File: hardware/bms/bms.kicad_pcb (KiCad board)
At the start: 4 copper layers, 120 x 45 mm, 287 parts, among them J1 Screw_Terminal_01x01, J10 Conn_01x10, J11 USB_C_Receptacle_USB2.0, J12 Conn_01x03, J13 Conn_01x07, J2 Screw_Terminal_01x01, J3 Screw_Terminal_01x01, J4 Screw_Terminal_01x01, J5 Screw_Terminal_01x01, J6 Conn_01x02, J7 Conn_01x10, J8 Conn_01x02, J9 Micro_SD_Card_Det2, Q1 MMBT3904, Q2 Q_PMOS_GSD, Q3 Q_PMOS_GSD, Q4 BSZ018N04LS6ATMA1, Q5 IAUC120N04S6N006ATMA1, Q6 IAUC120N04S6N006ATMA1, Q7 BSZ018N04LS6ATMA1, Q8 BSZ018N04LS6ATMA1, Q9 BSZ018N04LS6ATMA1, SW1 SW_SPST, SW2 SW_Push, SW3 SW_Push, U1 BQ76952, U2 LM74700, U3 BQ24610, U4 LM5166X, U5 TPS62172DSG, U6 ESP32-C3-MINI-1-N4, U8 USBLC6-2SC6, U9 TXU0101DCKR

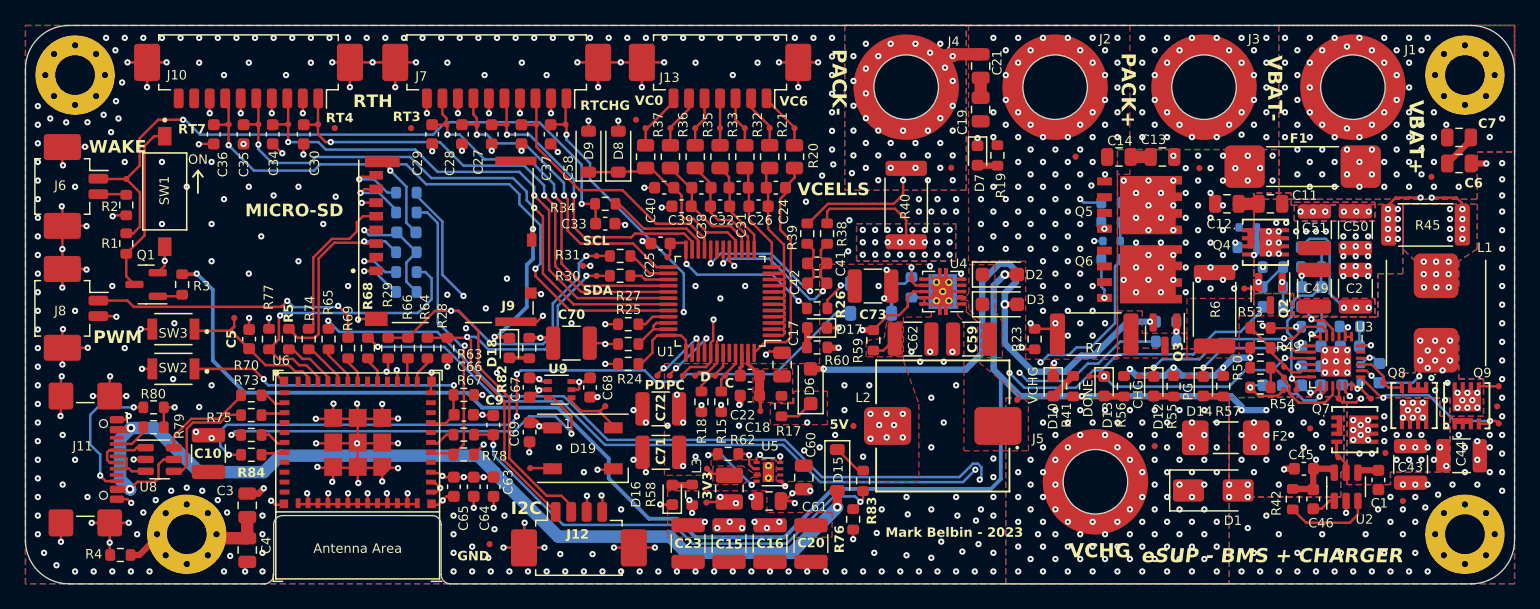
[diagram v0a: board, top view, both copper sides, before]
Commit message: Added keystone clip test points for ground, should be nice
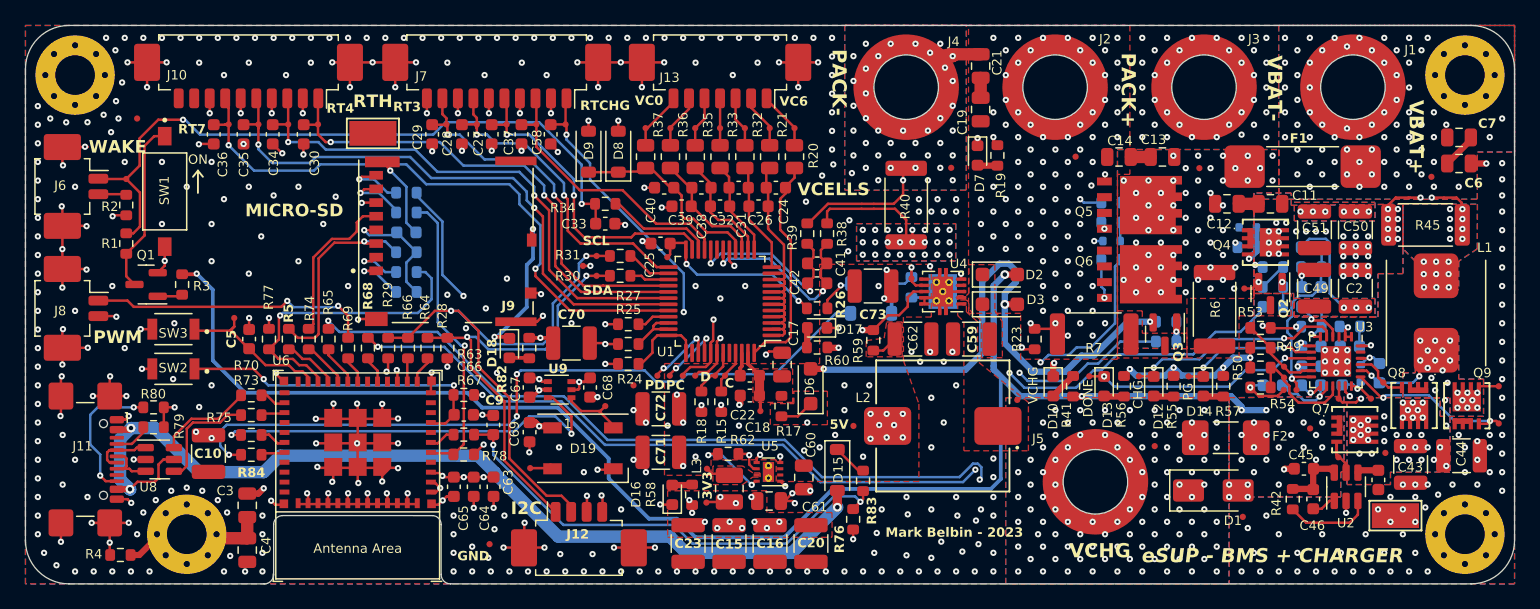
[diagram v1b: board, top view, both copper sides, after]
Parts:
- TP17, TP18: footprint bms:TestPoint_Pad_D0.5mm -> bms:TestPoint_Keystone_5019_Minature
- moved TP19 27.4 mm to (137.5, 104.0)
- moved TP17 21.2 mm to (116.5, 83.7)
- moved TP50 15.9 mm to (97.5, 82.5)
- moved TP52 13.0 mm to (186.6, 114.6)
- moved TP18 12.0 mm to (198.9, 114.5), turned to 180 degrees
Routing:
- net /BATTERY BALANCE AND MONITOR/PACK: track 56.0 -> 56.5 mm

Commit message: Updated silkscreen
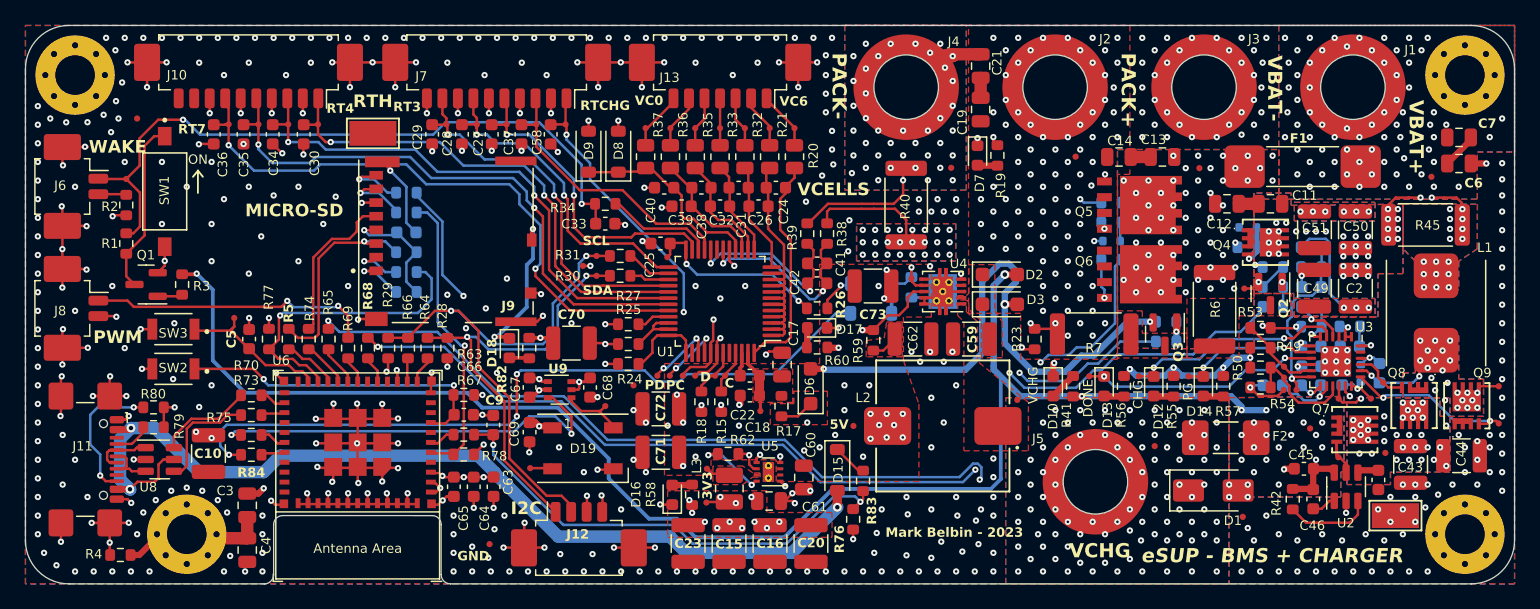
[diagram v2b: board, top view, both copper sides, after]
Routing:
- net GND: vias 521 -> 520
- net /VCHG_IN: vias 100 -> 95

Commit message: Review of BMS board looks good, finished!
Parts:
- moved C72 0.10 mm to (139.7, 106.0)
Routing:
- net GND: track 235.1 -> 234.2 mm
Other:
- board text added: "LP"
